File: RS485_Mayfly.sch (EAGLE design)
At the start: 13 parts, among them J1 TWIG-2.0-DIP, J2 TWIG-2.0-DIP, J3 TWIG-2.0-DIP, J5 CONN_42.54_NOSILK, J6 CONN_42.54_NOSILK, J7 CONN_42.54_NOSILK

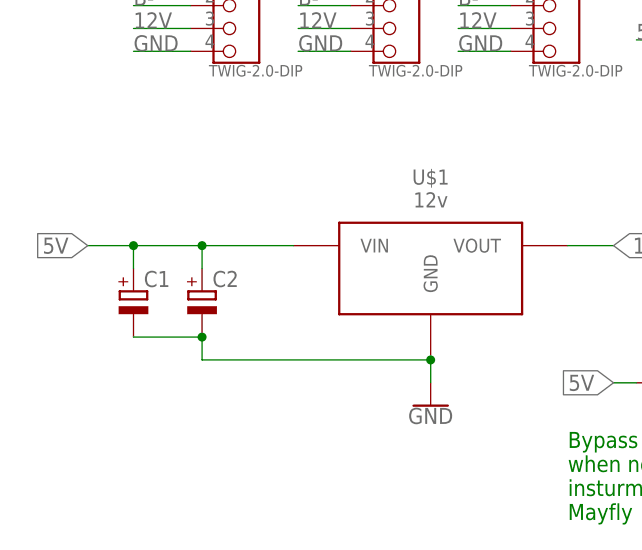
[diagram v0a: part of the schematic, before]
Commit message: Added board and schematic images
Added PNGs for both the PCB and the schematic for the Mrk1 design, adjusted noted in schematic design as well
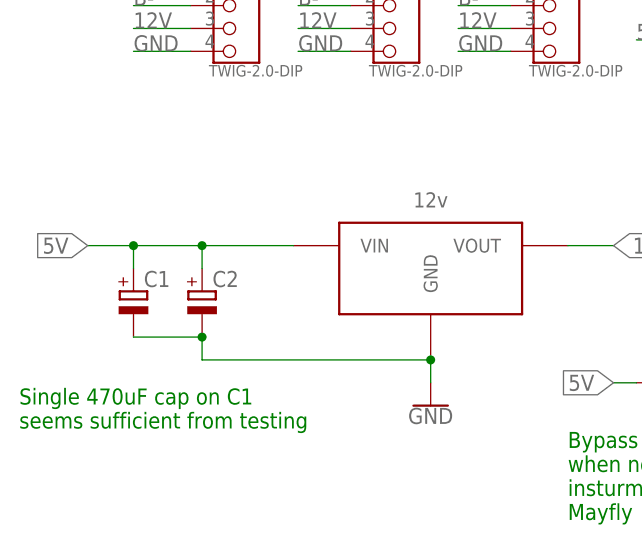
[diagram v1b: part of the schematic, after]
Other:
- note added: "Single 470uF cap on C1 seems sufficient from testing"
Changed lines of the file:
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@@
 insturment directly off of 5v from
 Mayfly</text>
+<text x="5.08" y="5.08" size="1.778" layer="91">Single 470uF cap on C1
+seems sufficient from testing</text>
 </plain>
 <instances>
 <instance part="C1" gate="G$1" x="17.78" y="20.32"/>
 <instance part="C2" gate="G$1" x="25.4" y="20.32"/>
-<instance part="U$1" gate="G$1" x="50.8" y="20.32"/>
+<instance part="U$1" gate="G$1" x="50.8" y="20.32" smashed="yes">
+<attribute name="VALUE" x="50.8" y="30.48" size="1.6764" layer="95" align="center"/>
+</instance>
 <instance part="U$2" gate="G$1" x="124.46" y="20.32"/>
 <instance part="J1" gate="G$1" x="27.94" y="50.8"/>
